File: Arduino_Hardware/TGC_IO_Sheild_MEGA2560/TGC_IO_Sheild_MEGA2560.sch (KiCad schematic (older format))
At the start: 28 parts

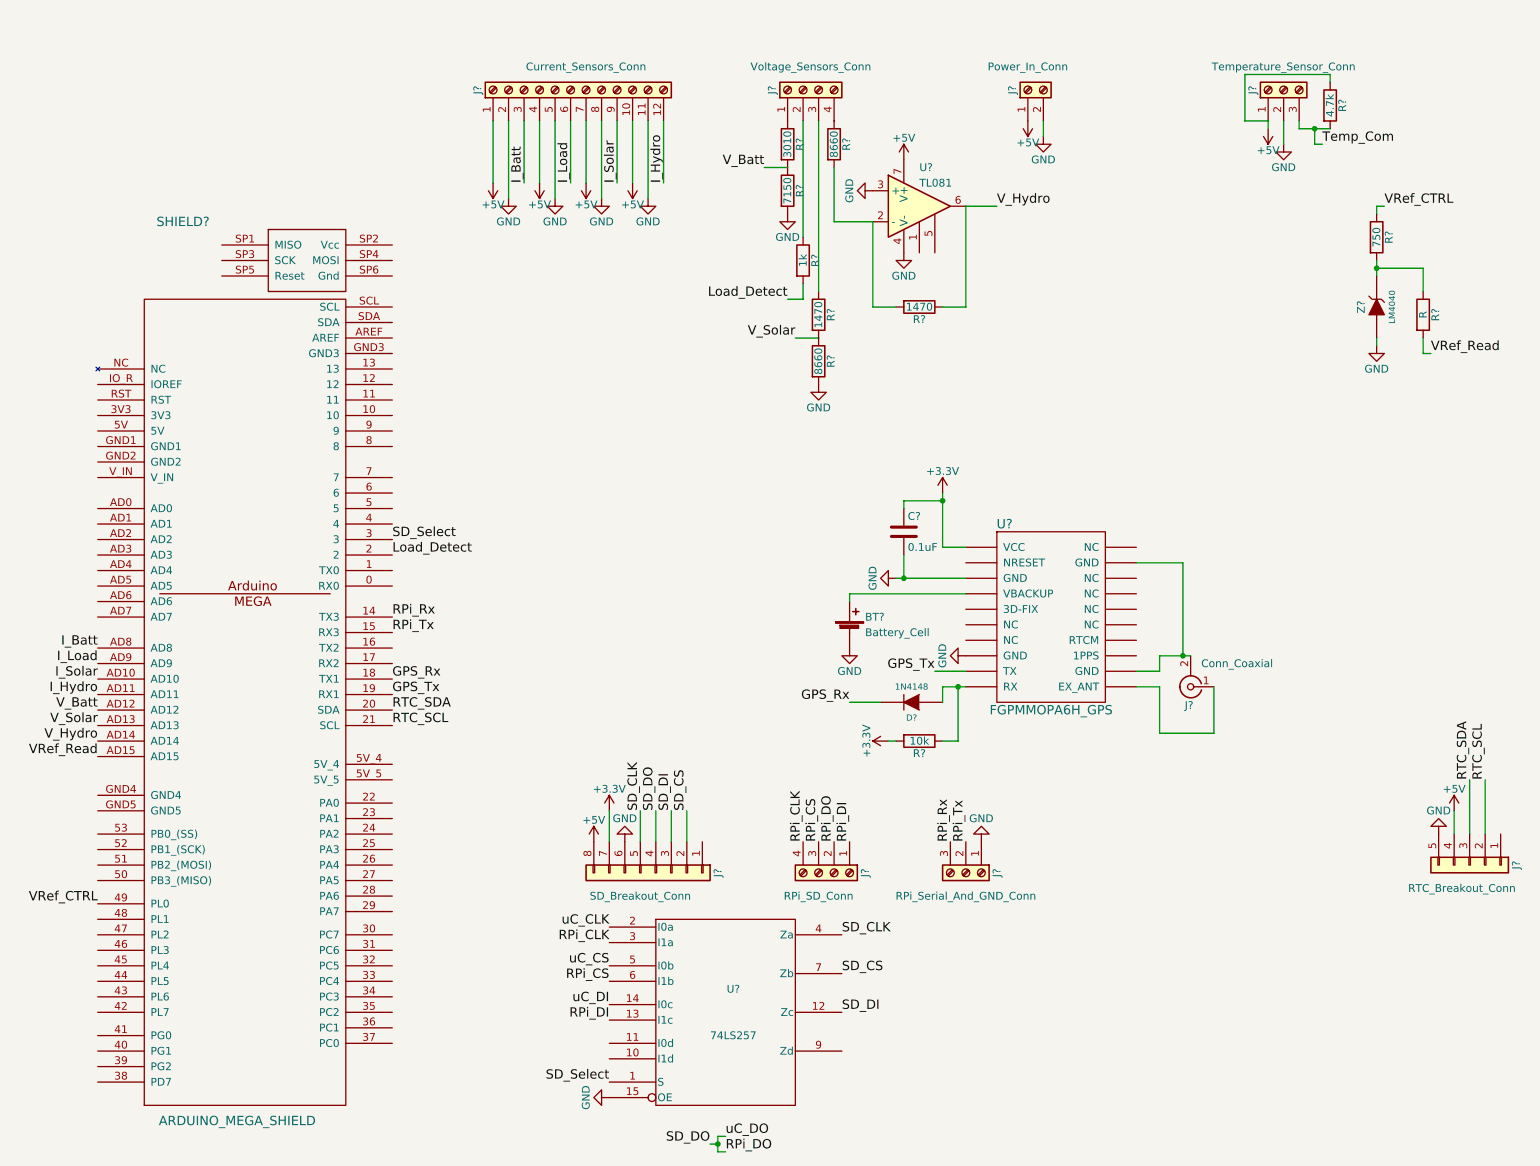
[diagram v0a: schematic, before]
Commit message: Pretty much restared everything because I forgot how it worked... New working folder is 'TGC_monitor'
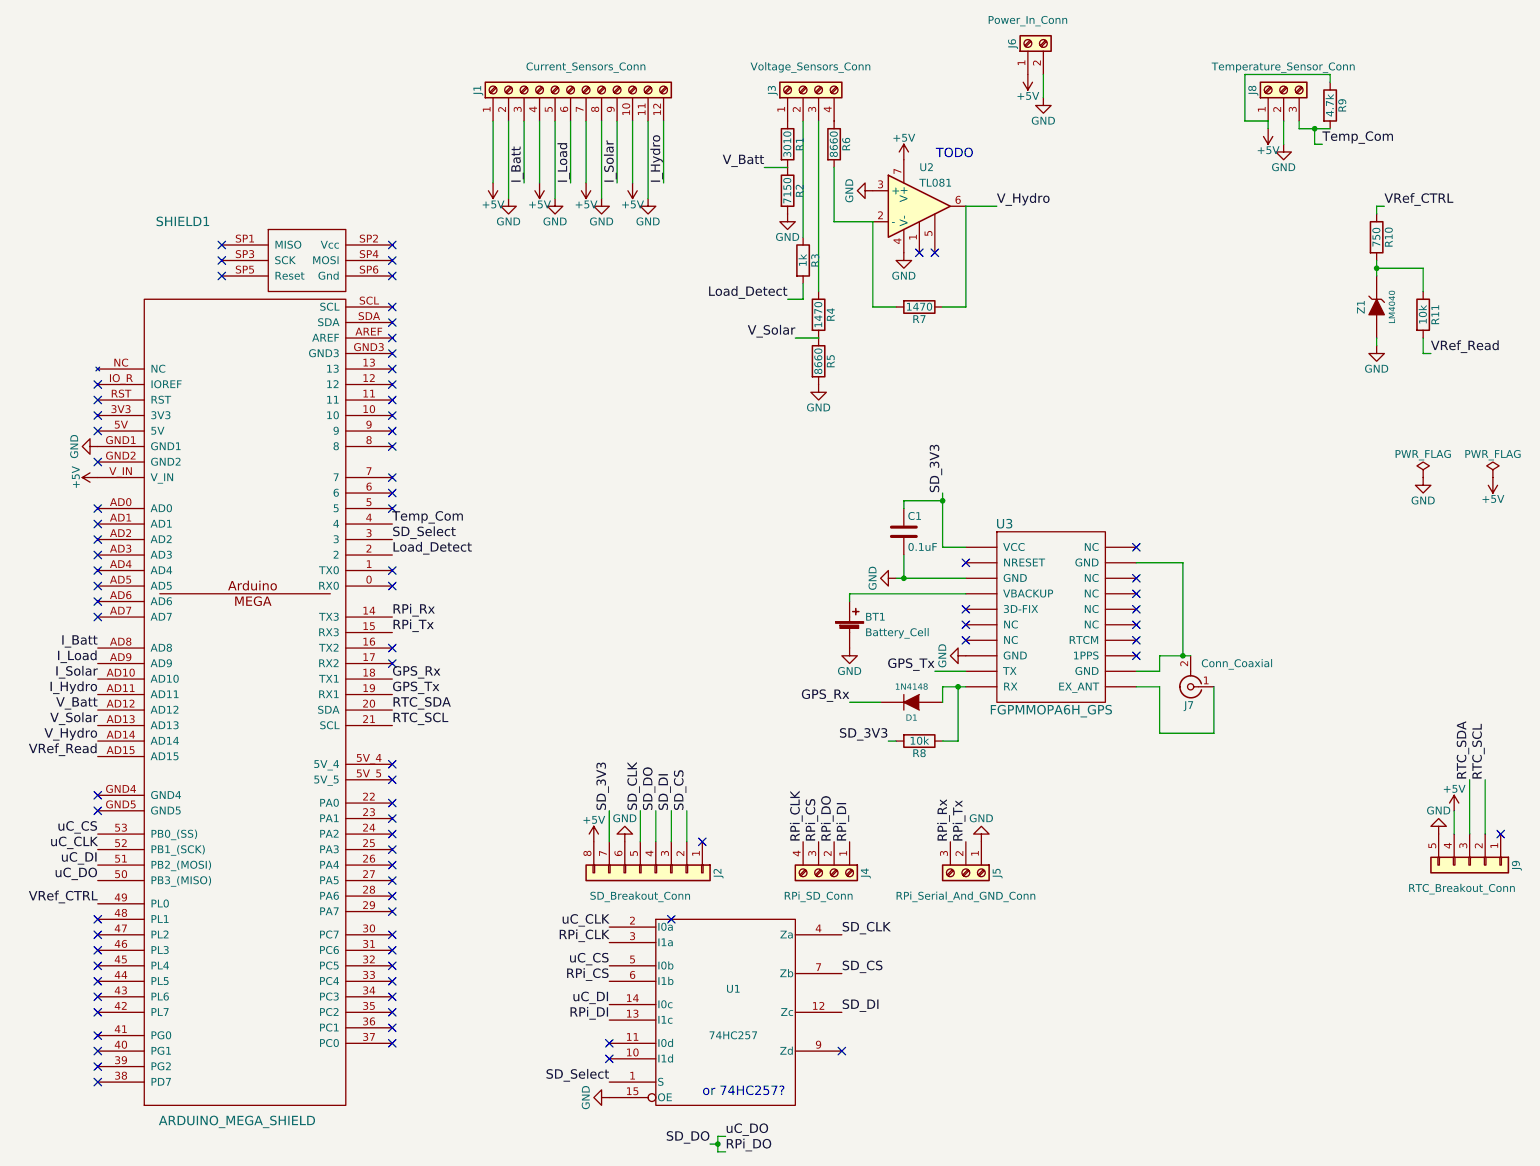
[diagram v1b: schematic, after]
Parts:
- R11: renamed from R?; value R -> 10k
- U1: renamed from U?; value 74LS257 -> 74HC257
- gave numbers to parts that had none: 26
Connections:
- net +3V3 is gone; now on net SD_3V3: C1.1, J2.7 (Pin_7), R8.2, U3.~ (VCC)
- net +5V: now also SHIELD1.V_IN
- net GND: now also SHIELD1.GND1
- net RPi_DO: now also SHIELD1.50 (PB3_(MISO))
- net Temp_Com: now also SHIELD1.4
- net uC_CLK: now also SHIELD1.52 (PB1_(SCK))
- net uC_CS: now also SHIELD1.53 (PB0_(SS))
- net uC_DI: now also SHIELD1.51 (PB2_(MOSI))
- net SD_3V3: now reaches U3.~ (VCC)
- no-connect marks 0 -> 86
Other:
- note added: "TODO"
- note added: "or 74HC257?"
- moved on the sheet: J6
